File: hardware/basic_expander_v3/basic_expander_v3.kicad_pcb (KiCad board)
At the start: 2 copper layers, 80 x 75 mm, 27 parts, among them J1 Daisy Pod, SW1 SW_Push, SW2 SW_Push, SW3 SW_Push, SW4 SW_Push, SW5 SW_Push, SW6 SW_Push, SW7 SW_Push, SW8 SW_Push, U1 4051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

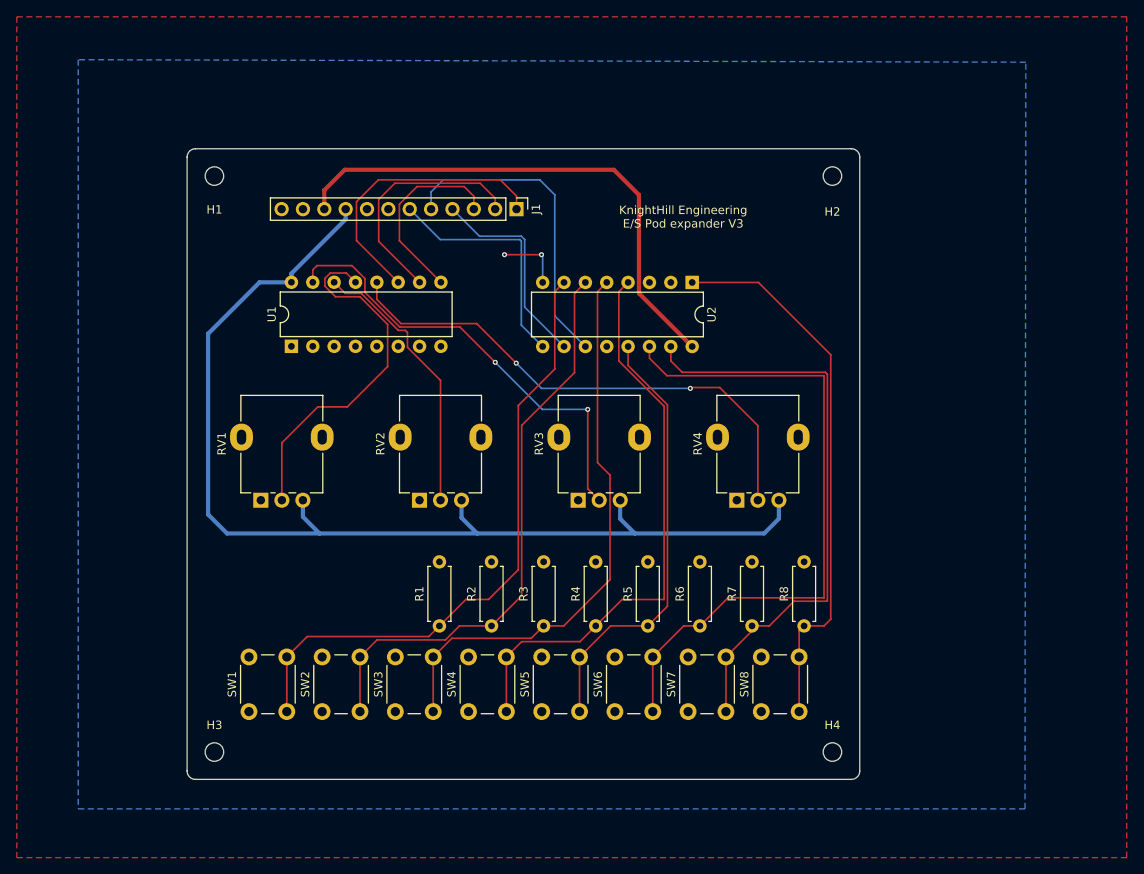
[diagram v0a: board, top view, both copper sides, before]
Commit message: add 4 pots
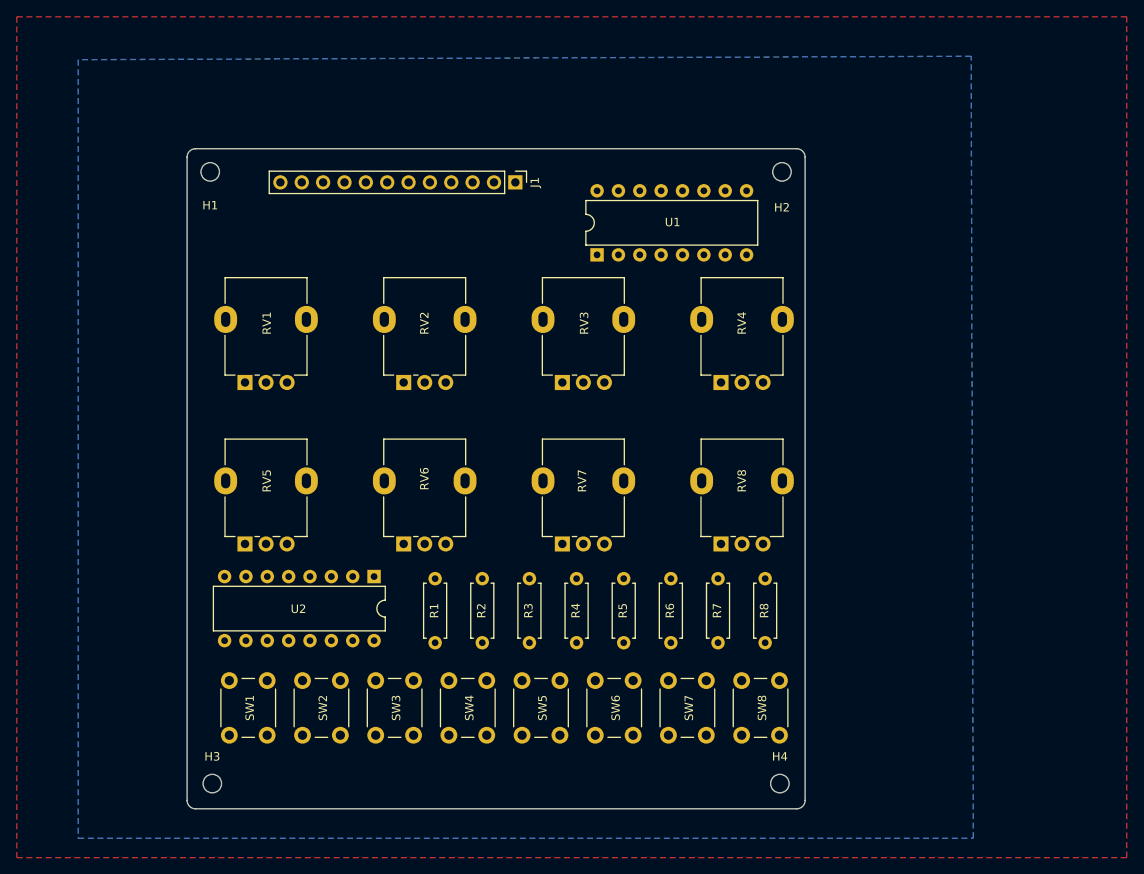
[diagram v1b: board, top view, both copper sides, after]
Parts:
- added RV5: 10k, Potentiometer_THT:Potentiometer_Alpha_RD901F-40-00D_Single_Vertical, F.Cu at (117.1, 132.7)
- added RV6: 10k, Potentiometer_THT:Potentiometer_Alpha_RD901F-40-00D_Single_Vertical, F.Cu at (136.0, 132.7)
- added RV7: 10k, Potentiometer_THT:Potentiometer_Alpha_RD901F-40-00D_Single_Vertical, F.Cu at (154.9, 132.7)
- added RV8: 10k, Potentiometer_THT:Potentiometer_Alpha_RD901F-40-00D_Single_Vertical, F.Cu at (173.8, 132.7)
- moved U2 51.5 mm to (132.5, 136.6)
- moved U1 37.9 mm to (159.0, 98.3)
- moved RV2 14.1 mm to (136.0, 113.5)
- moved RV3 14.1 mm to (154.9, 113.5)
- moved RV4 14.1 mm to (173.8, 113.5)
- moved RV1 14.1 mm to (117.1, 113.5)
- moved H4 7.29 mm to (180.8, 161.2)
- moved H2 6.02 mm to (181.0, 88.4)
- moved R8 5.04 mm to (179.0, 144.4)
- moved R7 4.51 mm to (173.4, 144.4)
- moved R6 3.99 mm to (167.8, 144.4)
- moved H3 3.76 mm to (113.2, 161.2)
- moved SW1 3.65 mm to (115.3, 155.4)
- moved SW3 3.65 mm to (132.7, 155.4)
- moved SW4 3.65 mm to (141.4, 155.4)
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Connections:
- U1 pad 1: unconnected-(U1-X4-Pad1) -> /RV1
- U1 pad 12: /RV4 -> /RV5
- U1 pad 13: /RV1 -> /RV6
- U1 pad 14: /RV2 -> /RV7
- U1 pad 15: /RV3 -> /RV8
- U1 pad 2: unconnected-(U1-X6-Pad2) -> /RV3
- U1 pad 4: unconnected-(U1-X7-Pad4) -> /RV4
- U1 pad 5: unconnected-(U1-X5-Pad5) -> /RV2
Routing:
- net VDDA: track 131.2 -> 0.00 mm
- net /SW6: track 79.2 -> 0.00 mm
- net /SW1: track 74.7 -> 0.00 mm
- net /SW7: track 69.6 -> 0.00 mm
- net /SW2: track 69.1 -> 0.00 mm
- net /SW4: track 68.5 -> 0.00 mm
- net /SW3: track 67.8 -> 0.00 mm
- net /SW8: track 65.4 -> 0.00 mm
- net VDD: track 62.6 -> 0.00 mm
- net /RV4: track 62.5 -> 0.00 mm, vias 2 -> 0
- net /RV3: track 53.8 -> 0.00 mm, vias 2 -> 0
- net /SW5: track 52.3 -> 0.00 mm
- net /RV1: track 42.8 -> 0.00 mm
- net /D11: track 37.6 -> 0.00 mm
- net /A: track 34.1 -> 0.00 mm
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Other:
- board size 80 x 75 mm -> 73.5 x 78.5 mm
- board text added: "KnightHill Engineering E/S Pod expander V3.1"
- board text removed: "KnightHill Engineering E/S Pod expander V3"

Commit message: add license
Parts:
- moved U2 19.3 mm to (114.8, 144.1), turned to 90 degrees
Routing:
- net /SW8: track 0.00 -> 99.4 mm
- net /SW7: track 0.00 -> 87.6 mm
- net /SW6: track 0.00 -> 64.4 mm
- net /SW3: track 0.00 -> 59.1 mm
- net /SW5: track 0.00 -> 54.3 mm
- net /SW2: track 0.00 -> 45.3 mm
- net /SW1: track 0.00 -> 32.0 mm
- net /SW4: track 0.00 -> 19.0 mm
